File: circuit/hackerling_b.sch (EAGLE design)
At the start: 45 parts, among them IC1 MCP23017SP, IC2 MCP2300X/P, IC3 MIC5219BM5, SW2 SWITCH_B13EH, U1 MMA8452Q, U2 LCD_16X2, U3 ARDUINOR3-BPLACE, U4 ACCELEROMETER, U5 PCA9306, U6 ACCELEROMETER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

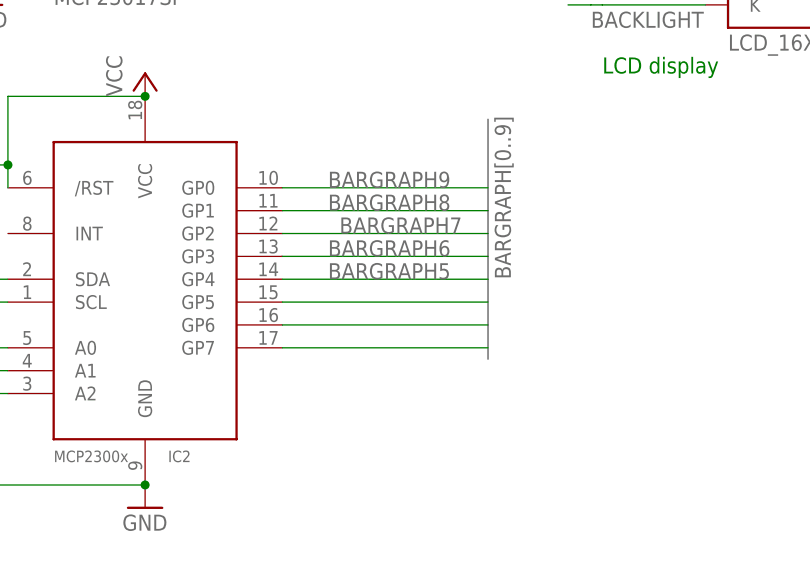
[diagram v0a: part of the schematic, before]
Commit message: made silkscreen and some cosmetic changes
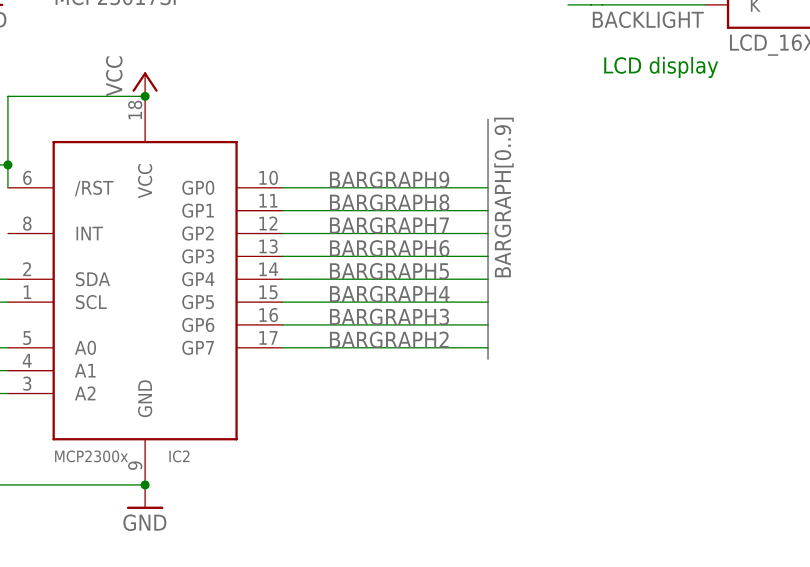
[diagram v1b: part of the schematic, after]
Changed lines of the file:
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@@
 <pinref part="IC2" gate="G$1" pin="GP7"/>
 <wire x1="182.88" y1="-17.78" x2="160.02" y2="-17.78" width="0.1524" layer="91"/>
+<label x="165.1" y="-17.78" size="1.778" layer="95"/>
 </segment>
 </net>
@@
 <pinref part="IC2" gate="G$1" pin="GP6"/>
 <wire x1="182.88" y1="-15.24" x2="160.02" y2="-15.24" width="0.1524" layer="91"/>
+<label x="165.1" y="-15.24" size="1.778" layer="95"/>
 </segment>
 </net>
@@
 <pinref part="IC2" gate="G$1" pin="GP5"/>
 <wire x1="182.88" y1="-12.7" x2="160.02" y2="-12.7" width="0.1524" layer="91"/>
+<label x="165.1" y="-12.7" size="1.778" layer="95"/>
 </segment>
 </net>
@@
 <pinref part="IC2" gate="G$1" pin="GP2"/>
 <wire x1="160.02" y1="-5.08" x2="182.88" y2="-5.08" width="0.1524" layer="91"/>
-<label x="166.37" y="-5.08" size="1.778" layer="95"/>
+<label x="165.1" y="-5.08" size="1.778" layer="95"/>
 </segment>
 </net>

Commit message: changes made for version 1.2. ordered boards.
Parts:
- added C5: (no value), rcl:CPOL-USE5-4
- added U$2: HS-LOGOSMALL, hackerscouts:HS-LOGOSMALL
- C4: device rcl:C-US050-050X075 -> hackerscouts:CAP_050X075
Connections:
- net DIP1 renamed DIP4
- net DIPR1 renamed DIPR4
- net 3.3V: now also U1.NC_15, U1.NC_16, U1.SAO
- net DIP2: now also RN2C.2, SW1.3; no longer RN2B.2, SW1.2
- net DIP3: now also RN2B.2, SW1.2; no longer RN2C.2, SW1.3
- net DIPR2: now also IC1.GPA3, RN2C.1; no longer IC1.GPA2, RN2B.1
- net DIPR3: now also IC1.GPA2, RN2B.1; no longer IC1.GPA3, RN2C.1
- net GND: now also C4.-, C5.-, U1.NC_8; no longer C4.2, IC1.A1, IC2.A1, U1.SAO
- net N$19: now also C4.+; no longer C4.1
- net N$26: now also C5.+
- net VCC: now also IC1.A1, IC2.A1
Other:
- note added: "Optional Capacitor Show what a signal looks like with cap"
- moved on the sheet: C2

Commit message: adding version 1.3 schematics
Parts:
- removed JP1, JP2: (no value), SparkFun:M02LOCK
- removed U$2: HS-LOGOSMALL, hackerscouts:HS-LOGOSMALL
- added HACKERSCOUTSLOGO: HS-LOGO, hackerscouts:HS-LOGO
- added JP3: (no value), SparkFun:M02LOCK
- added U$1: M04X2, SparkFun:M04X2
- SERVO1: value (none) -> SERVO
- renumbered SERVO2 to SERVO
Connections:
- new net RX: JP3.2, U3.D0
- new net TX: JP3.1, U3.D1
- net GND: now also U$1.5, U$1.6; no longer JP1.2, JP2.2
- net N$24: now also U$1.4; no longer JP1.1
- net N$26: now also U$1.3; no longer JP2.1
- net SVO1: now also U$1.7
- net SVO2: now also U$1.8
- net TEMP: now also U$1.1
- net VCC: now also U$1.2
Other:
- note added: "JP1"
- note added: "JP2"
- note removed: "Btn1"
- note removed: "Btn2"
- note removed: "Btn3"
- note removed: "Btn4"
- note removed: "Unconnected"
- moved on the sheet: LED2, LED3, RN4
